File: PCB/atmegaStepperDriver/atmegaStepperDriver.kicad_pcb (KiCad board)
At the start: 2 copper layers, 50.8 x 92.1 mm, 83 parts, among them J1 General power, J2 Motor Output, J3 Motor power, J4 Conn_01x02_Pin, J5 Reset Header, J6 I2C Communication pins, J8 Conn_01x06_Socket, J9 Stepper communication pins, Q1 TIP42C, Q10 BC547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

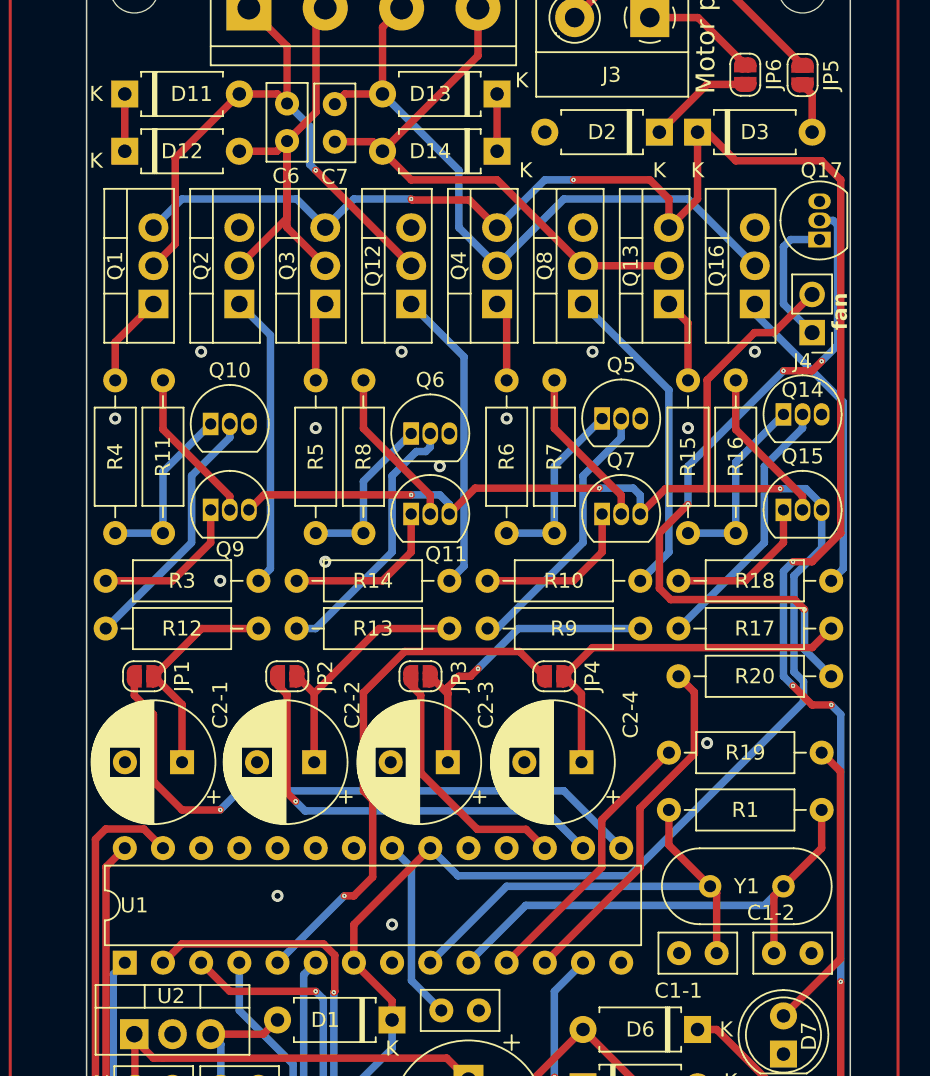
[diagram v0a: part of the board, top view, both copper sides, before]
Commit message: fixed bad transistors; readme; V0.8.3
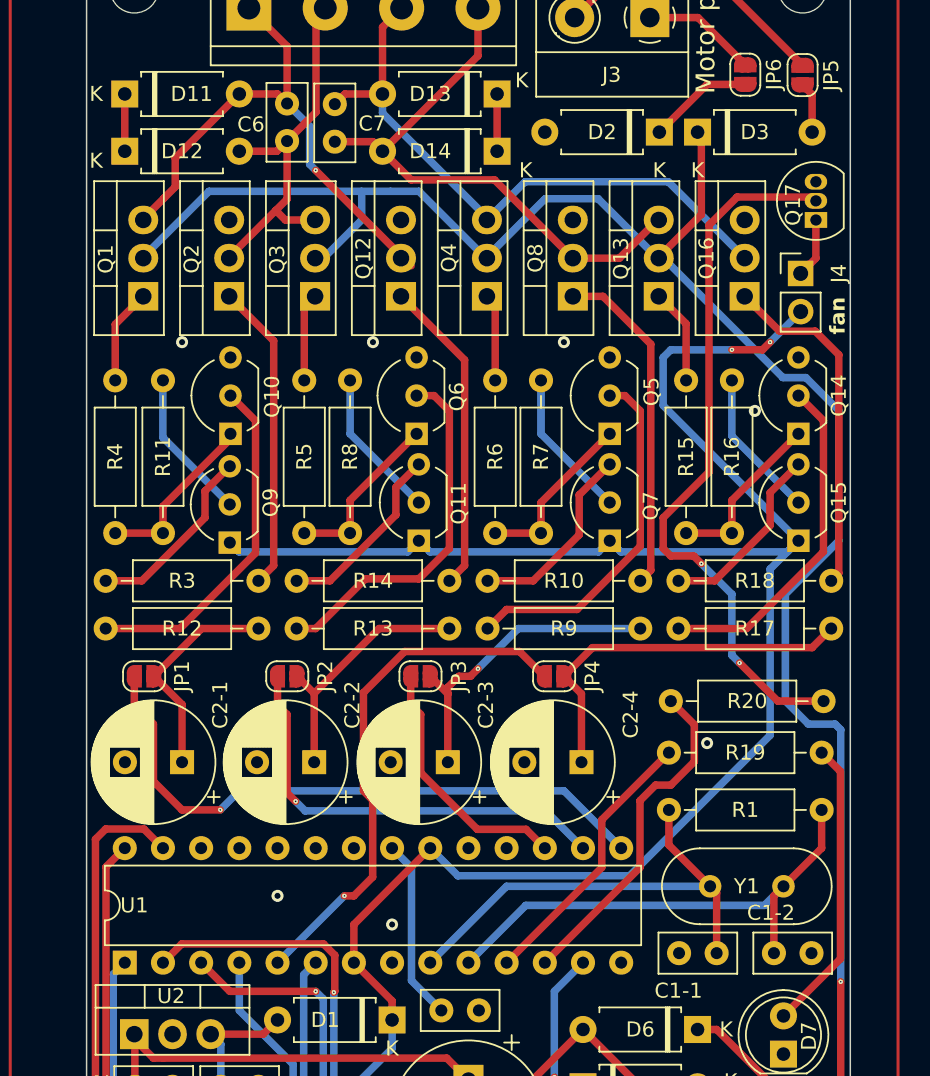
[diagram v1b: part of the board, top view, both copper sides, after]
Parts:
- Q10, Q11, Q14, Q15, Q5, Q6, Q7, Q9: footprint Package_TO_SOT_THT:TO-92_Inline -> Package_TO_SOT_THT:TO-92_Inline_Wide
- R20: value 50 -> 250
- moved R12 10.2 mm to (73.7, 97.8), turned to 0 degrees
- moved R3 10.2 mm to (83.8, 94.6), turned to 180 degrees
- moved J4 4.01 mm to (119.9, 74.2), turned to 0 degrees
- moved Q9 2.52 mm to (81.9, 92.1), turned to 90 degrees
- moved Q15 2.28 mm to (119.7, 91.9), turned to 90 degrees
- moved Q11 1.85 mm to (94.5, 91.9), turned to 90 degrees
- moved Q7 1.85 mm to (107.2, 91.9), turned to 90 degrees
- moved R20 1.73 mm to (111.3, 102.6)
- moved Q14 1.63 mm to (119.7, 84.8), turned to 90 degrees
- moved Q10 1.47 mm to (82.0, 84.8), turned to 90 degrees
- moved Q17 1.32 mm to (120.9, 70.6)
- moved Q5 1.14 mm to (107.2, 84.8), turned to 90 degrees
- moved R8 0.89 mm to (89.9, 91.4)
- moved R7 0.89 mm to (102.6, 91.4)
- moved Q12 0.85 mm to (93.3, 75.7)
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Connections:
- Q1 pad 2: output A -> Motor Power
- Q1 pad 3: Motor Power -> output A
- Q11 pad 1: Net-(Q11-C) -> +5V
- Q11 pad 3: +5V -> Net-(Q11-E)
- Q13 pad 2: output !B -> Motor Power
- Q13 pad 3: Motor Power -> output !B
- Q15 pad 1: Net-(Q15-C) -> +5V
- Q15 pad 3: +5V -> Net-(Q15-E)
- Q3 pad 2: output !A -> Motor Power
- Q3 pad 3: Motor Power -> output !A
- Q4 pad 2: output B -> Motor Power
- Q4 pad 3: Motor Power -> output B
- Q7 pad 1: Net-(Q7-C) -> +5V
- Q7 pad 3: +5V -> Net-(Q7-E)
- Q9 pad 1: Net-(Q9-C) -> +5V
- Q9 pad 3: +5V -> Net-(Q9-E)
- R10 pad 1: Net-(Q7-C) -> Net-(Q7-E)
- R12 pad 1: Gate 1 -> Net-(Q10-B)
- R12 pad 2: Net-(Q10-B) -> Gate 1
- R14 pad 1: Net-(Q11-C) -> Net-(Q11-E)
- R18 pad 1: Net-(Q15-C) -> Net-(Q15-E)
- R3 pad 1: Net-(Q9-C) -> Net-(Q2-B)
- R3 pad 2: Net-(Q2-B) -> Net-(Q9-E)
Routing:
- net Net-(Q7-E): track 0.00 -> 12.9 mm
- net Net-(Q15-E): track 0.00 -> 12.5 mm
- net Net-(Q9-E): track 0.00 -> 12.4 mm
- net Net-(Q11-E): track 0.00 -> 12.4 mm
- net Net-(Q7-C): track 10.9 -> 0.00 mm
- net Net-(Q11-C): track 10.9 -> 0.00 mm
- net Net-(Q9-C): track 10.2 -> 0.00 mm
- net Net-(Q15-C): track 10.2 -> 0.00 mm
- net Net-(Q6-B): track 17.8 -> 24.1 mm
- net Net-(Q10-B): track 17.0 -> 23.2 mm
- net output !A: track 31.6 -> 25.6 mm
- net Net-(Q5-B): track 18.0 -> 23.9 mm
- net Net-(Q14-B): track 17.7 -> 22.8 mm
- net Net-(J4-Pin_1): track 9.10 -> 3.98 mm
- net output B: track 45.1 -> 41.3 mm
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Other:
- board text added: "atMega Stepper Driver V0.8.3"
- board text removed: "atMega Stepper Driver V0.8.2"

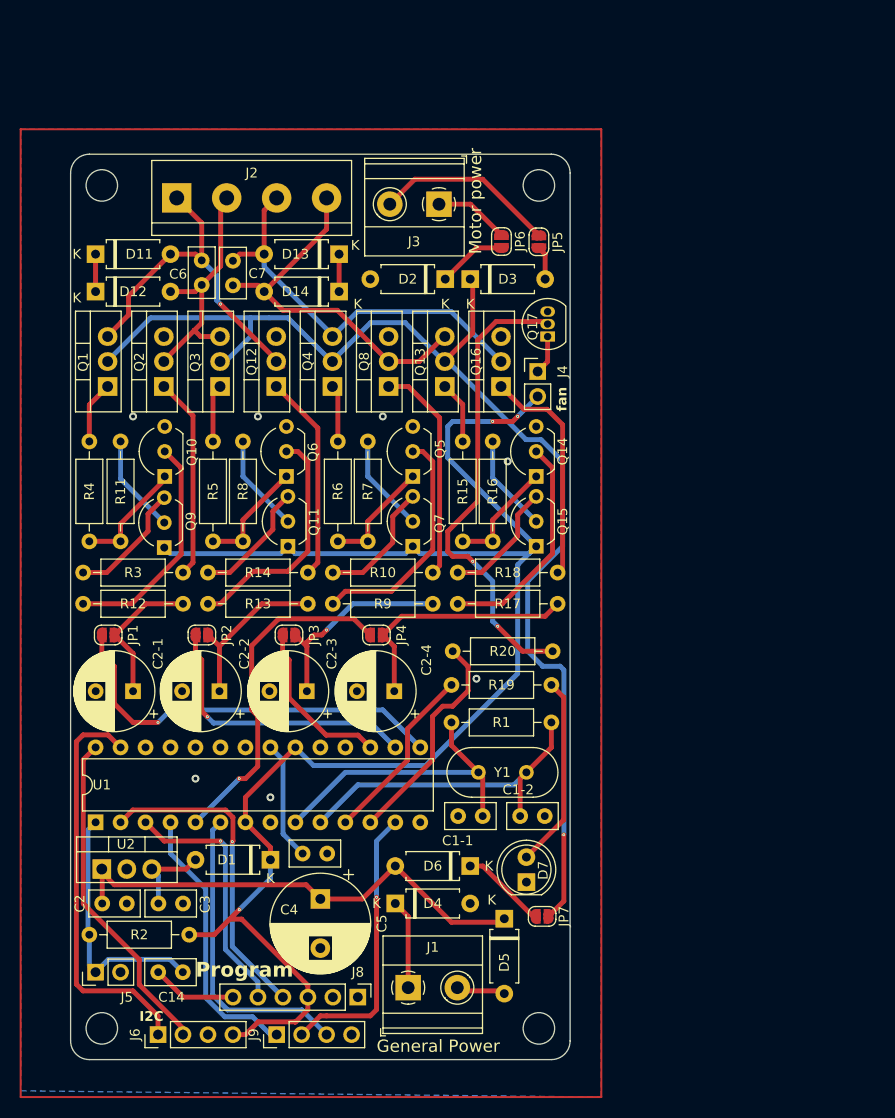
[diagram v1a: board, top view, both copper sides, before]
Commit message: Fix gate; added termistor; gate sheet added; v0.8.4
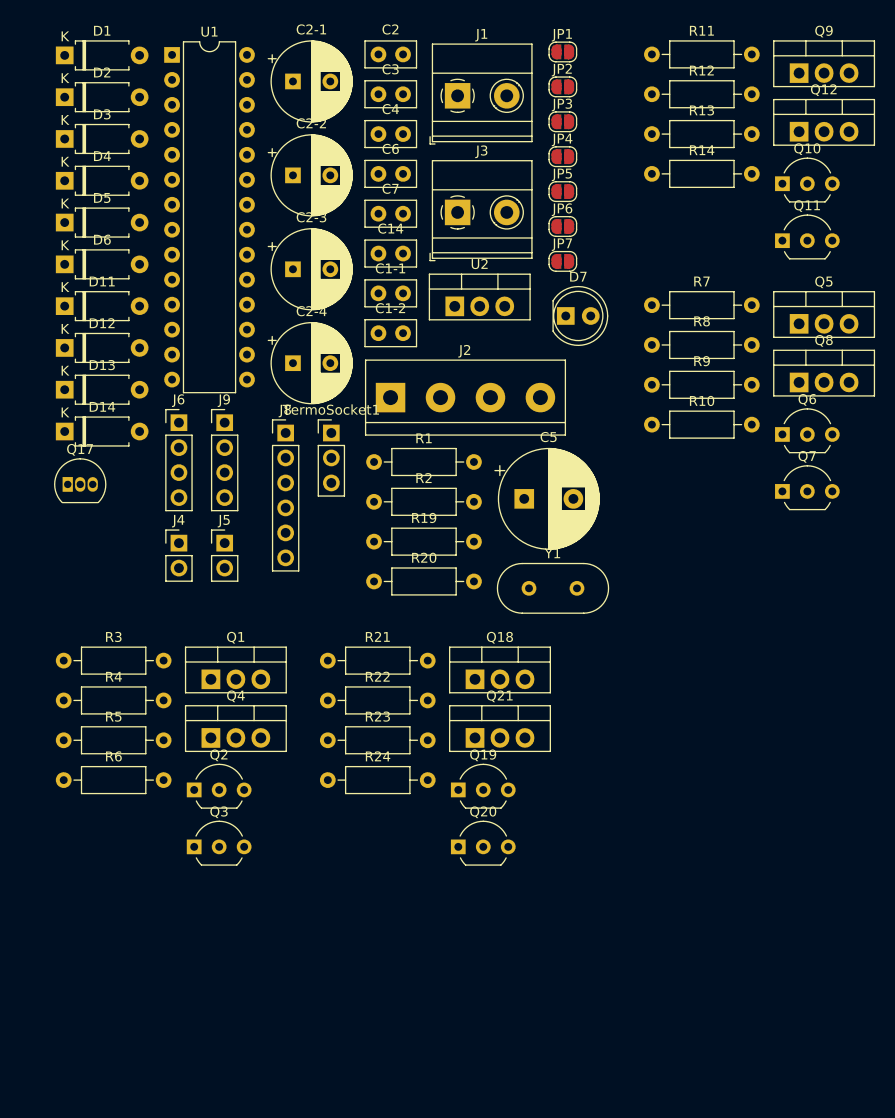
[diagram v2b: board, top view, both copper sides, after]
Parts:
- removed Q13: TIP42C, Package_TO_SOT_THT:TO-220-3_Vertical
- removed Q14: BC547, Package_TO_SOT_THT:TO-92_Inline_Wide
- removed Q15: BC557, Package_TO_SOT_THT:TO-92_Inline_Wide
- removed Q16: TIP41C, Package_TO_SOT_THT:TO-220-3_Vertical
- removed R15, R18: 50, Resistor_THT:R_Axial_DIN0207_L6.3mm_D2.5mm_P10.16mm_Horizontal
- removed R16, R17: 1k, Resistor_THT:R_Axial_DIN0207_L6.3mm_D2.5mm_P10.16mm_Horizontal
- removed REF** (x4): MountingHole_3.2mm_M3_DIN965, MountingHole:MountingHole_3.2mm_M3_DIN965
- added Q18: TIP42C, Package_TO_SOT_THT:TO-220-3_Vertical, F.Cu at (113.5, 105.5)
- added Q19: BC557, Package_TO_SOT_THT:TO-92_Inline_Wide, F.Cu at (111.8, 116.7)
- added Q20: BC547, Package_TO_SOT_THT:TO-92_Inline_Wide, F.Cu at (111.8, 122.5)
- added Q21: TIP41C, Package_TO_SOT_THT:TO-220-3_Vertical, F.Cu at (113.5, 111.4)
- added R21: 50, Resistor_THT:R_Axial_DIN0207_L6.3mm_D2.5mm_P10.16mm_Horizontal, F.Cu at (98.5, 103.6)
- added R22: 1k, Resistor_THT:R_Axial_DIN0207_L6.3mm_D2.5mm_P10.16mm_Horizontal, F.Cu at (98.5, 107.6)
- added R23: 1k, Resistor_THT:R_Axial_DIN0207_L6.3mm_D2.5mm_P10.16mm_Horizontal, F.Cu at (98.5, 111.7)
- added R24: 50, Resistor_THT:R_Axial_DIN0207_L6.3mm_D2.5mm_P10.16mm_Horizontal, F.Cu at (98.5, 115.7)
- added TermoSocket1: Conn_01x03_Pin, Connector_PinHeader_2.54mm:PinHeader_1x03_P2.54mm_Vertical, F.Cu at (98.9, 80.4)
- J4: value Conn_01x02_Pin -> FanSocket
- J8: value Conn_01x06_Socket -> Programming socket 01x06
- Q10, Q6: value BC547 -> BC557
- Q11, Q7: value BC557 -> BC547
- Q2: value TIP41C -> BC557; footprint Package_TO_SOT_THT:TO-220-3_Vertical -> Package_TO_SOT_THT:TO-92_Inline_Wide
- Q3: value TIP42C -> BC547; footprint Package_TO_SOT_THT:TO-220-3_Vertical -> Package_TO_SOT_THT:TO-92_Inline_Wide
- Q4: value TIP42C -> TIP41C
- Q5: value BC547 -> TIP42C; footprint Package_TO_SOT_THT:TO-92_Inline_Wide -> Package_TO_SOT_THT:TO-220-3_Vertical
- Q9: value BC557 -> TIP42C; footprint Package_TO_SOT_THT:TO-92_Inline_Wide -> Package_TO_SOT_THT:TO-220-3_Vertical
- R11, R7: value 1k -> 50
- R4, R5: value 50 -> 1k
- moved J1 90.8 mm to (111.8, 46.1)
- moved C2 90.1 mm to (103.7, 41.9), turned to 0 degrees
- moved C3 84.7 mm to (103.7, 46.0), turned to 0 degrees
- moved D1 84.4 mm to (71.8, 42.0), turned to 0 degrees
- moved D5 83.7 mm to (71.8, 59.0), turned to 0 degrees
- moved D4 80.8 mm to (71.8, 54.8)
- moved Q9 80.6 mm to (146.5, 43.8), turned to 0 degrees
- moved U1 78.4 mm to (82.7, 42.0), turned to 0 degrees
- moved R12 77.7 mm to (131.5, 46.0)
- moved C14 76.4 mm to (103.7, 62.2)
- moved JP1 75.2 mm to (122.5, 41.7), turned to 0 degrees
- moved D6 73.8 mm to (71.8, 63.3), turned to 0 degrees
- moved C4 73.4 mm to (103.7, 50.0), turned to 0 degrees
- moved R11 73.3 mm to (131.5, 41.9), turned to 0 degrees
- moved Q10 69.5 mm to (144.8, 55.1), turned to 0 degrees
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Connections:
- Q1 pad 2: Motor Power -> output !A
- Q1 pad 3: output A -> Motor Power
- Q10 pad 3: GND -> +5V
- Q11 pad 1: +5V -> Net-(Q11-C)
- Q11 pad 3: Net-(Q11-E) -> GND
- Q12 pad 2: output A -> output B
- Q2 pad 1: Net-(Q2-B) -> Net-(Q2-C)
- Q2 pad 2: output !A -> Net-(Q2-B)
- Q2 pad 3: GND -> +5V
- Q3 pad 1: Net-(Q3-B) -> Net-(Q3-C)
- Q3 pad 2: Motor Power -> Net-(Q3-B)
- Q3 pad 3: output !A -> GND
- Q4 pad 2: Motor Power -> output A
- Q4 pad 3: output B -> GND
- Q5 pad 1: Net-(Q5-C) -> Net-(Q5-B)
- Q5 pad 2: Net-(Q5-B) -> output B
- Q5 pad 3: GND -> Motor Power
- Q6 pad 3: GND -> +5V
- Q7 pad 1: +5V -> Net-(Q7-C)
- Q7 pad 3: Net-(Q7-E) -> GND
- Q9 pad 1: +5V -> Net-(Q9-B)
- Q9 pad 2: Net-(Q9-B) -> output !B
- Q9 pad 3: Net-(Q9-E) -> Motor Power
- R10 pad 1: Net-(Q7-E) -> Net-(Q8-B)
- R10 pad 2: Net-(Q8-B) -> Net-(Q6-C)
- R11 pad 1: Net-(Q10-C) -> Net-(Q9-B)
- R11 pad 2: Net-(Q9-B) -> Net-(Q11-C)
- R12 pad 1: Net-(Q10-B) -> Net-(Q11-C)
- R12 pad 2: Gate 1 -> Net-(Q10-B)
- R13 pad 1: Gate 2 -> Net-(Q11-B)
- R13 pad 2: Net-(Q6-B) -> Gate 4
- R14 pad 1: Net-(Q11-E) -> Net-(Q12-B)
- R14 pad 2: Net-(Q12-B) -> Net-(Q10-C)
- R3 pad 1: Net-(Q2-B) -> Net-(Q1-B)
- R3 pad 2: Net-(Q9-E) -> Net-(Q3-C)
- R4 pad 1: Net-(Q1-B) -> Net-(Q3-C)
- R4 pad 2: Net-(Q10-C) -> Net-(Q2-B)
- R5 pad 2: Net-(Q6-C) -> Gate 2
- R6 pad 2: Net-(Q5-C) -> Net-(Q2-C)
- R7 pad 1: Net-(Q5-C) -> Net-(Q5-B)
- R7 pad 2: Net-(Q7-B) -> Net-(Q7-C)
- R8 pad 1: Net-(Q6-C) -> Net-(Q7-C)
- R8 pad 2: Net-(Q11-B) -> Net-(Q6-B)
- R9 pad 1: Gate 3 -> Net-(Q7-B)
- R9 pad 2: Net-(Q5-B) -> Gate 3
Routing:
- net +5V: track 155.9 -> 0.00 mm, vias 3 -> 0
- net Motor Power: track 124.2 -> 0.00 mm, vias 1 -> 0
- net VCCInput: track 49.8 -> 0.00 mm
- net Net-(Q17-B): track 48.0 -> 0.00 mm, vias 2 -> 0
- net Net-(JP1-B): track 41.5 -> 0.00 mm, vias 1 -> 0
- net SDA: track 41.5 -> 0.00 mm
- net output B: track 41.3 -> 0.00 mm
- net output !B: track 38.0 -> 0.00 mm
- net output A: track 36.1 -> 0.00 mm, vias 1 -> 0
- net Jumper To lower Pins: track 35.1 -> 0.00 mm, vias 1 -> 0
- net SCL: track 33.9 -> 0.00 mm
- net Net-(U1-XTAL2/PB7): track 33.9 -> 0.00 mm
- net RXD: track 32.7 -> 0.00 mm, vias 1 -> 0
- net Net-(U1-XTAL1/PB6): track 31.6 -> 0.00 mm
- net Error: track 31.1 -> 0.00 mm
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- removed copper zone on B.Cu, net GND
- removed copper zone on F.Cu, net GND
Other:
- board outline removed
- board text removed: "General Power"
- board text removed: "I2C"
- board text removed: "Motor power"
- board text removed: "Program"
- board text removed: "atMega Stepper Driver V0.8.3"
- board text removed: "fan"
